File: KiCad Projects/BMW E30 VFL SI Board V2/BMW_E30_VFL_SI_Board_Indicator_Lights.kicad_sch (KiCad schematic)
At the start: 14 parts, among them J1 Conn_01x13_Pin, Q5 BC337-25, Q6 BC337-25, Q7 BC337-25

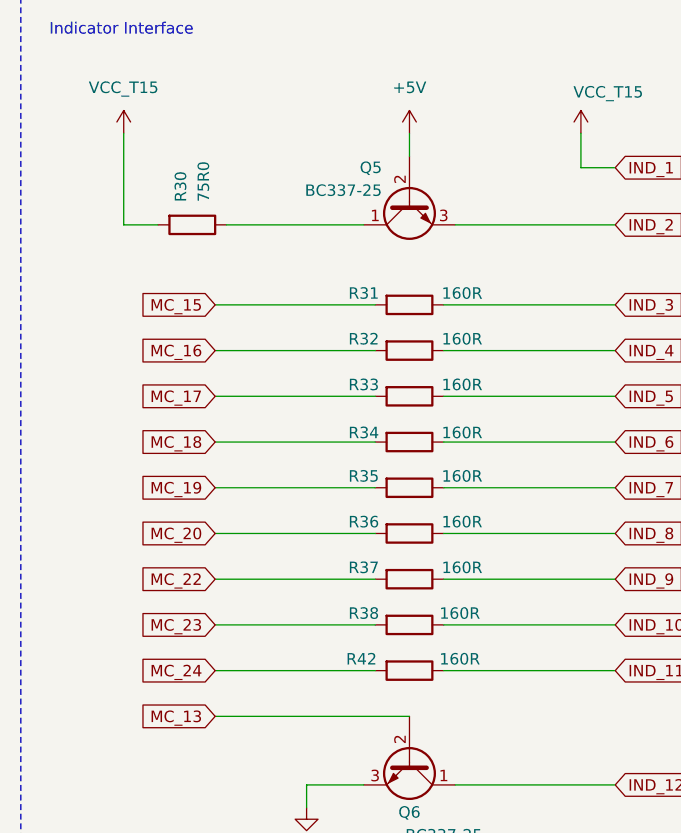
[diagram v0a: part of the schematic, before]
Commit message: Bugfixing of component designators
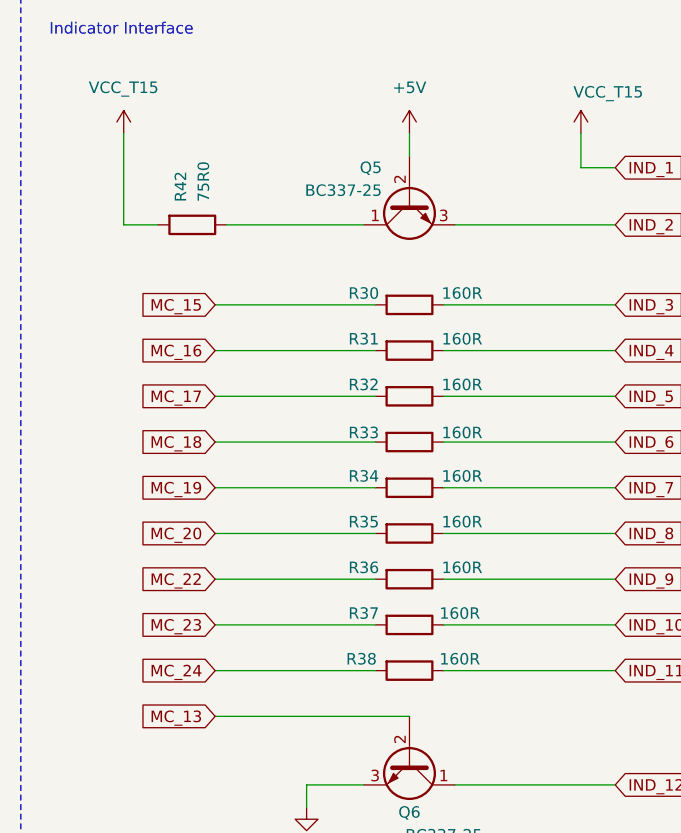
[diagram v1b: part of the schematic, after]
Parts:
- renumbered R31 to R30, R32 to R31, R33 to R32, R34 to R33, R35 to R34, R36 to R35, R37 to R36, R38 to R37, R42 to R38, R30 to R42
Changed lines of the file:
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@@
 		(on_board yes)
 		(dnp no)
-		(property "Reference" "R34"
+		(property "Reference" "R33"
 			(at 97.79 80.264 90)
 			(effects
@@
 			(project "BMW E30 VFL SI Board V2"
 				(path "/b9f8b657-f23f-4f46-b33b-c9c07ea00dca/6ab6acf9-4780-467c-9f6a-c9ea57cd95e1"
-					(reference "R34")
+					(reference "R33")
 					(unit 1)
 				)
@@
 		(on_board yes)
 		(dnp no)
-		(property "Reference" "R36"
+		(property "Reference" "R35"
 			(at 97.79 90.17 90)
 			(effects
@@
 			(project "BMW E30 VFL SI Board V2"
 				(path "/b9f8b657-f23f-4f46-b33b-c9c07ea00dca/6ab6acf9-4780-467c-9f6a-c9ea57cd95e1"
-					(reference "R36")
+					(reference "R35")
 					(unit 1)
 				)
@@
 		(on_board yes)
 		(dnp no)
-		(property "Reference" "R42"
+		(property "Reference" "R38"
 			(at 97.536 105.41 90)
 			(effects
@@
 			(project "BMW E30 VFL SI Board V2"
 				(path "/b9f8b657-f23f-4f46-b33b-c9c07ea00dca/6ab6acf9-4780-467c-9f6a-c9ea57cd95e1"
-					(reference "R42")
+					(reference "R38")
 					(unit 1)
 				)
@@
 		(on_board yes)
 		(dnp no)
-		(property "Reference" "R33"
+		(property "Reference" "R32"
 			(at 97.79 74.93 90)
 			(effects
@@
 			(project "BMW E30 VFL SI Board V2"
 				(path "/b9f8b657-f23f-4f46-b33b-c9c07ea00dca/6ab6acf9-4780-467c-9f6a-c9ea57cd95e1"
-					(reference "R33")
+					(reference "R32")
 					(unit 1)
 				)
@@
 		(on_board yes)
 		(dnp no)
-		(property "Reference" "R37"
+		(property "Reference" "R36"
 			(at 97.79 95.25 90)
 			(effects
@@
 			(project "BMW E30 VFL SI Board V2"
 				(path "/b9f8b657-f23f-4f46-b33b-c9c07ea00dca/6ab6acf9-4780-467c-9f6a-c9ea57cd95e1"
-					(reference "R37")
+					(reference "R36")
 					(unit 1)
 				)
@@
 		(on_board yes)
 		(dnp no)
-		(property "Reference" "R31"
+		(property "Reference" "R30"
 			(at 97.79 64.77 90)
 			(effects
@@
 			(project "BMW E30 VFL SI Board V2"
 				(path "/b9f8b657-f23f-4f46-b33b-c9c07ea00dca/6ab6acf9-4780-467c-9f6a-c9ea57cd95e1"
-					(reference "R31")
+					(reference "R30")
 					(unit 1)
 				)
@@
 		(on_board yes)
 		(dnp no)
-		(property "Reference" "R35"
+		(property "Reference" "R34"
 			(at 97.79 85.09 90)
 			(effects
@@
 			(project "BMW E30 VFL SI Board V2"
 				(path "/b9f8b657-f23f-4f46-b33b-c9c07ea00dca/6ab6acf9-4780-467c-9f6a-c9ea57cd95e1"
-					(reference "R35")
+					(reference "R34")
 					(unit 1)
 				)
@@
 		(on_board yes)
 		(dnp no)
-		(property "Reference" "R38"
+		(property "Reference" "R37"
 			(at 97.79 100.33 90)
 			(effects
@@
 			(project "BMW E30 VFL SI Board V2"
 				(path "/b9f8b657-f23f-4f46-b33b-c9c07ea00dca/6ab6acf9-4780-467c-9f6a-c9ea57cd95e1"
-					(reference "R38")
+					(reference "R37")
 					(unit 1)
 				)
@@
 		(on_board yes)
 		(dnp no)
-		(property "Reference" "R32"
+		(property "Reference" "R31"
 			(at 97.79 69.85 90)
 			(effects
@@
 			(project "BMW E30 VFL SI Board V2"
 				(path "/b9f8b657-f23f-4f46-b33b-c9c07ea00dca/6ab6acf9-4780-467c-9f6a-c9ea57cd95e1"
-					(reference "R32")
+					(reference "R31")
 					(unit 1)
 				)
@@
 		(on_board yes)
 		(dnp no)
-		(property "Reference" "R30"
+		(property "Reference" "R42"
 			(at 77.47 54.61 0)
 			(effects
@@
 			(project "BMW E30 VFL SI Board V2"
 				(path "/b9f8b657-f23f-4f46-b33b-c9c07ea00dca/6ab6acf9-4780-467c-9f6a-c9ea57cd95e1"
-					(reference "R30")
-					(unit 1)
-				)
+					(reference "R42")
+					(unit 1)
+				)
